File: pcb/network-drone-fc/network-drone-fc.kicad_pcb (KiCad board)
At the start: 4 copper layers, 36 x 39 mm, 94 parts, among them J1 U.FL-R-SMT-1, J2 TYPE-C 16PIN 2MD, J3 U.FL GPS, J4 ESC, J5 Sensor port 5V I2C, J6 Radio UART 5V, J7 Charging board, J8 Landing sensor 5V I2C, U1 ESP32-S3FN8, U2 USBLC6-2SC6, U3 AP63205WU-7, U4 TLV75733PDRVR, U5 TPS7A2033PDBVR, U6 ICM-42688-P, U7 BMP581, U8 MAX-M10S, X1 FA-128 40MHz 10pF

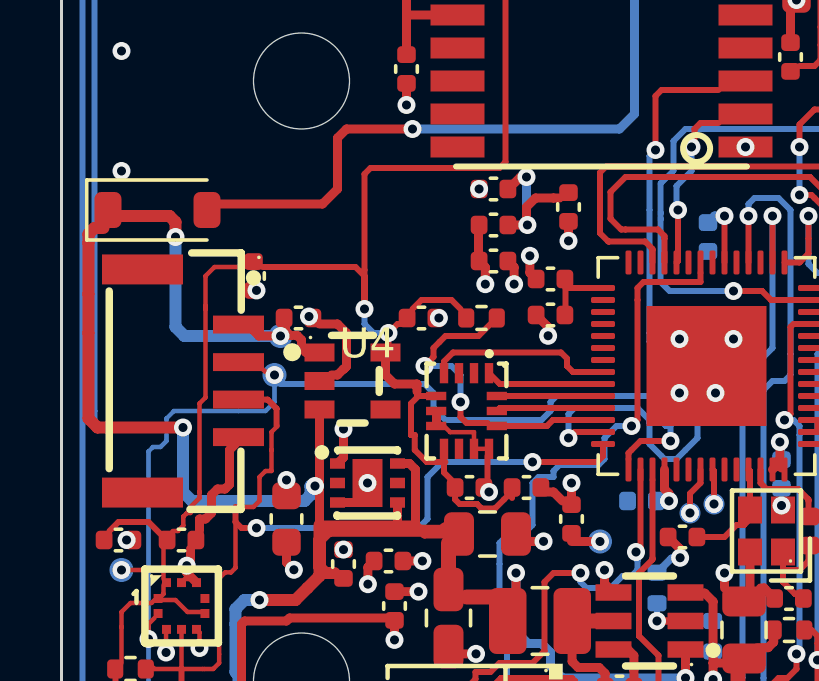
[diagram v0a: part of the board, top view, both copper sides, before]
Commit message: Vias moved out of six small capacitor pads (C4, C6, C22, C23, C25, C26) so they cannot drain the solder
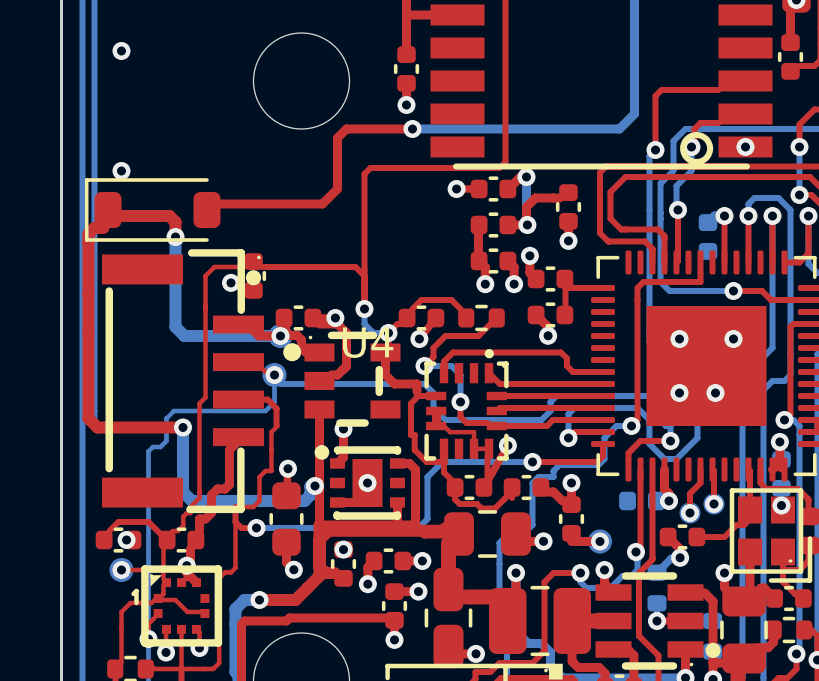
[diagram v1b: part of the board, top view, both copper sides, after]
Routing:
- net GND: track 74.9 -> 78.9 mm
- net +3V3: track 24.3 -> 25.4 mm
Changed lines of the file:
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@@
+	)
+	(segment
+		(start 96.08 103.55)
+		(end 96.88 102.149999)
+		(width 0.25)
+		(layer "F.Cu")
+		(net 2)
 	)
 	(segment
@@
 	)
 	(segment
+		(start 94.48 97.9)
+		(end 93.93 98.6)
+		(width 0.25)
+		(layer "F.Cu")
+		(net 2)
+	)
+	(segment
 		(start 87.6 103.449999)
 		(end 87.6 102.3)
@@
 	)
 	(segment
+		(start 90.38 97.9)
+		(end 91.13 97.9)
+		(width 0.25)
+		(layer "F.Cu")
+		(net 2)
+	)
+	(segment
+		(start 88.4 96.98)
+		(end 87.65 96.73)
+		(width 0.25)
+		(layer "F.Cu")
+		(net 2)
+	)
+	(segment
 		(start 115 114.5)
 		(end 116.5 114.5)
@@
 	)
 	(via
-		(at 94.58 97.9)
+		(at 93.93 98.6)
 		(size 0.6)
 		(drill 0.3)
@@
 	)
 	(via
-		(at 96.25 103.7)
+		(at 96.88 102.149999)
 		(size 0.6)
 		(drill 0.3)
@@
 	)
 	(via
-		(at 90.25 97.85)
-		(size 0.6)
-		(drill 0.3)
-		(layers "F.Cu" "B.Cu")
-		(net 2)
-	)
-	(via
-		(at 88.5 96.98)
+		(at 91.13 97.9)
+		(size 0.6)
+		(drill 0.3)
+		(layers "F.Cu" "B.Cu")
+		(net 2)
+	)
+	(via
+		(at 87.65 96.73)
 		(size 0.6)
 		(drill 0.3)
@@
 	)
 	(segment
+		(start 89.5 103.825)
+		(end 89.55 102.925)
+		(width 0.25)
+		(layer "F.Cu")
+		(net 5)
+	)
+	(segment
 		(start 89.6 107.9)
 		(end 92.8 107.9)
@@
 	(segment
 		(start 89.5 103.825)
-		(end 89.5 103.3)
+		(end 89.5 103.825)
 		(width 0.3)
 		(layer "F.Cu")
@@
 		(end 106 102.9)
 		(width 0.3)
+		(layer "F.Cu")
+		(net 5)
+	)
+	(segment
+		(start 95.92 93.6)
+		(end 95.17 93.6)
+		(width 0.25)
 		(layer "F.Cu")
 		(net 5)
@@
 	)
 	(via
-		(at 89.5 103.3)
+		(at 89.55 102.925)
 		(size 0.6)
 		(drill 0.3)
@@
 	)
 	(via
-		(at 95.92 93.6)
-		(size 0.6)
-		(drill 0.3)
+		(at 95.17 93.6)
+		(size 0.6)
+		(drill 0.3)

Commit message: Five more ground vias in the ESP32's exposed pad, nine in all as Espressif recommends
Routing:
- net GND: vias 74 -> 79
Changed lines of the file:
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@@
+	)
+	(via
+		(at 103.5 98.6)
+		(size 0.6)
+		(drill 0.3)
+		(layers "F.Cu" "B.Cu")
+		(net 2)
+	)
+	(via
+		(at 104 99.5)
+		(size 0.6)
+		(drill 0.3)
+		(layers "F.Cu" "B.Cu")
+		(net 2)
 	)
 	(via
@@
 	)
 	(via
+		(at 104 101.05)
+		(size 0.6)
+		(drill 0.3)
+		(layers "F.Cu" "B.Cu")
+		(net 2)
+	)
+	(via
 		(at 108.83 101.797372)
 		(size 0.6)
@@
 	)
 	(via
+		(at 102.2 97.9)
+		(size 0.6)
+		(drill 0.3)
+		(layers "F.Cu" "B.Cu")
+		(net 2)
+	)
+	(via
 		(at 108 117)
 		(size 0.6)
@@
 		(size 0.6)
 		(drill 0.3)
+		(layers "F.Cu" "B.Cu")
+		(net 2)
+	)
+	(via
+		(at 105 97.9)
+		(size 0.6)
+		(drill 0.3)

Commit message: Top-side ground pour, with ground vias to keep its islands and blocked-spoke pads left on their own tracks
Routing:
- net GND: vias 79 -> 91
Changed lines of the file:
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@@
 			(roundrect_rratio 0.25)
 			(net 2 "GND")
+			(zone_connect 0)
 		)
 		(embedded_fonts no)
@@
 			(roundrect_rratio 0.25)
 			(net 2 "GND")
+			(zone_connect 0)
 		)
 		(embedded_fonts no)
@@
 			(roundrect_rratio 0.25)
 			(net 2 "GND")
+			(zone_connect 0)
 		)
 		(embedded_fonts no)
@@
 			(roundrect_rratio 0.25)
 			(net 2 "GND")
+			(zone_connect 0)
 		)
 		(embedded_fonts no)
@@
 			(roundrect_rratio 0.25)
 			(net 2 "GND")
+			(zone_connect 0)
 		)
 		(embedded_fonts no)
@@
 			(layers "F.Cu" "F.Mask" "F.Paste")
 			(net 2 "GND")
+			(zone_connect 0)
 		)
 		(pad "12" smd rect
@@
 			(layers "F.Cu" "F.Mask" "F.Paste")
 			(net 2 "GND")
+			(zone_connect 0)
 		)
 		(embedded_fonts no)
@@
 	)
 	(via
+		(at 84.950499 98.981947)
+		(size 0.6)
+		(drill 0.3)
+		(layers "F.Cu" "B.Cu")
+		(net 2)
+	)
+	(via
+		(at 89.830687 101.727897)
+		(size 0.6)
+		(drill 0.3)
+		(layers "F.Cu" "B.Cu")
+		(net 2)
+	)
+	(via
 		(at 84.17 105.3)
 		(size 0.6)
@@
 	)
 	(via
+		(at 101.405648 114.777791)
+		(size 0.6)
+		(drill 0.3)
+		(layers "F.Cu" "B.Cu")
+		(net 2)
+	)
+	(via
 		(at 106 104.15)
 		(size 0.6)
@@
 	)
 	(via
+		(at 106.492791 90.524378)
+		(size 0.6)
+		(drill 0.3)
+		(layers "F.Cu" "B.Cu")
+		(net 2)
+	)
+	(via
+		(at 104.671281 112.9255)
+		(size 0.6)
+		(drill 0.3)
+		(layers "F.Cu" "B.Cu")
+		(net 2)
+	)
+	(via
 		(at 92 113)
 		(size 0.6)
@@
 	)
 	(via
+		(at 89.038865 95.088574)
+		(size 0.6)
+		(drill 0.3)
+		(layers "F.Cu" "B.Cu")
+		(net 2)
+	)
+	(via
 		(at 92.2 103.4)
 		(size 0.6)
@@
 	)
 	(via
+		(at 111.294078 86.989274)
+		(size 0.6)
+		(drill 0.3)
+		(layers "F.Cu" "B.Cu")
+		(net 2)
+	)
+	(via
 		(at 96 81)
 		(size 0.6)
@@
 	)
 	(via
+		(at 94.0505 95.5505)
+		(size 0.6)
+		(drill 0.3)
+		(layers "F.Cu" "B.Cu")
+		(net 2)
+	)
+	(via
 		(at 116 97)
 		(size 0.6)
@@
 	)
 	(via
+		(at 103.390955 93.9505)
+		(size 0.6)
+		(drill 0.3)
+		(layers "F.Cu" "B.Cu")
+		(net 2)
+	)
+	(via
+		(at 102.6505 91.0505)
+		(size 0.6)
+		(drill 0.3)
+		(layers "F.Cu" "B.Cu")
+		(net 2)
+	)
+	(via
+		(at 86.437259 111.294221)
+		(size 0.6)
+		(drill 0.3)
+		(layers "F.Cu" "B.Cu")
+		(net 2)
+	)
+	(via
 		(at 93.899999 107.02)
 		(size 0.6)
@@
 	)
 	(via
+		(at 99.815247 95.94632)
+		(size 0.6)
+		(drill 0.3)
+		(layers "F.Cu" "B.Cu")
+		(net 2)
+	)
+	(via
 		(at 84 93)
 		(size 0.6)
@@
 		(hatch edge 0.5)
 		(connect_pads
-			(clearance 0.2)
+			(clearance 0.25)
 		)
-		(min_thickness 0.2)
+		(min_thickness 0.25)
 		(filled_areas_thickness no)
 		(fill yes
-			(thermal_gap 0.2)
+			(thermal_gap 0.3)
 			(thermal_bridge_width 0.3)
 		)
+		(polygon
+			(pts
+				(xy 82 79) (xy 118 79) (xy 118 118) (xy 82 118)
+			)
+		)
 	)

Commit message: Ground stitching vias along both RF traces
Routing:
- net GND: vias 91 -> 103
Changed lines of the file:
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@@
+	)
+	(via
+		(at 90.8 85.95)
+		(size 0.6)
+		(drill 0.3)
+		(layers "F.Cu" "B.Cu")
+		(net 2)
 	)
 	(via
@@
 	)
 	(via
+		(at 93.7 83.55)
+		(size 0.6)
+		(drill 0.3)
+		(layers "F.Cu" "B.Cu")
+		(net 2)
+	)
+	(via
 		(at 114.8 97.873)
 		(size 0.6)
@@
 	)
 	(via
+		(at 86 84.65)
+		(size 0.6)
+		(drill 0.3)
+		(layers "F.Cu" "B.Cu")
+		(net 2)
+	)
+	(via
 		(at 108.46 112.3)
 		(size 0.6)
@@
 	)
 	(via
+		(at 92.6 84.45)
+		(size 0.6)
+		(drill 0.3)
+		(layers "F.Cu" "B.Cu")
+		(net 2)
+	)
+	(via
 		(at 116 105)
 		(size 0.6)
@@
 	)
 	(via
+		(at 90.8 84.45)
+		(size 0.6)
+		(drill 0.3)
+		(layers "F.Cu" "B.Cu")
+		(net 2)
+	)
+	(via
+		(at 87.15 86.5)
+		(size 0.6)
+		(drill 0.3)
+		(layers "F.Cu" "B.Cu")
+		(net 2)
+	)
+	(via
+		(at 92.55 86.025)
+		(size 0.6)
+		(drill 0.3)
+		(layers "F.Cu" "B.Cu")
+		(net 2)
+	)
+	(via
 		(at 113.5 85.6)
 		(size 0.6)
@@
 	)
 	(via
+		(at 88.3 86.5)
+		(size 0.6)
+		(drill 0.3)
+		(layers "F.Cu" "B.Cu")
+		(net 2)
+	)
+	(via
+		(at 110.275 107.2)
+		(size 0.6)
+		(drill 0.3)
+		(layers "F.Cu" "B.Cu")
+		(net 2)
+	)
+	(via
+		(at 109.375 107.2)
+		(size 0.6)
+		(drill 0.3)
+		(layers "F.Cu" "B.Cu")
+		(net 2)
+	)
+	(via
 		(at 97.612944 95.827259)
 		(size 0.6)
@@
 	)
 	(via
+		(at 89.9 85.95)
+		(size 0.6)
+		(drill 0.3)
+		(layers "F.Cu" "B.Cu")
+		(net 2)
+	)
+	(via
 		(at 116 97)
 		(size 0.6)
 		(drill 0.3)
+		(layers "F.Cu" "B.Cu")
+		(net 2)
+	)
+	(via
+		(at 89.9 84.45)
+		(size 0.6)
+		(drill 0.3)
